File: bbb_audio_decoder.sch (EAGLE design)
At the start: 186 parts, among them IC1 OPA2134, IC2 LM317, IC3 LM337, IC4 OPA2134, IC5 OPA2134, IC6 OPA2134, IC7 LM317, P1 PLR135/T9, Q2 BS170, U1 PCM1690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

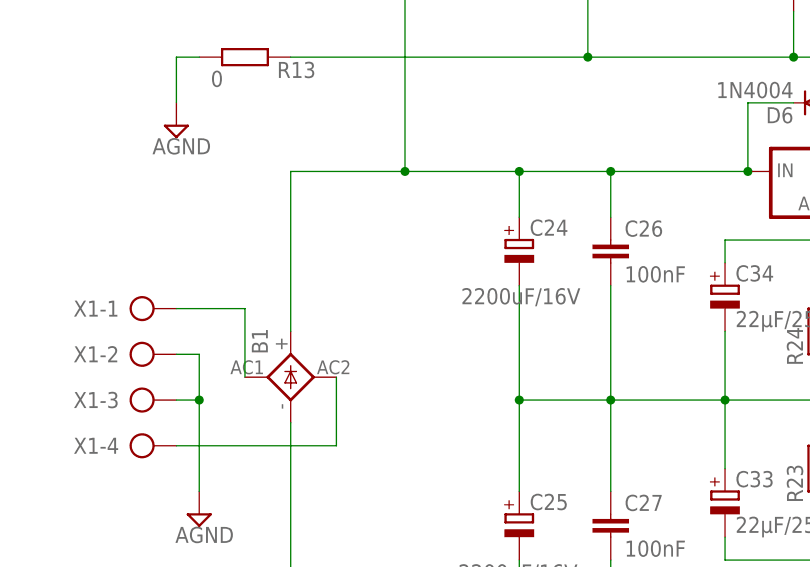
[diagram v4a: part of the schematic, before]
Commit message: Add another power supply cap to fix boot problems
The extra cap (C17) is 2200µF.

The problem was that it sometimes refused to boot. I saw the
BeagleBone's blue lights go off again when the boot process was
initiated. The LCD backlight dipped. Scope image revealved dips in the
rail, together with 100Hz rectification ripple. As a hack to my build, I
added 4700µF before the positive regulators.  That prevented the
dips. I'm not sure if this one extra 2200µF is enough though. Probably
it is, and there are space constraints.
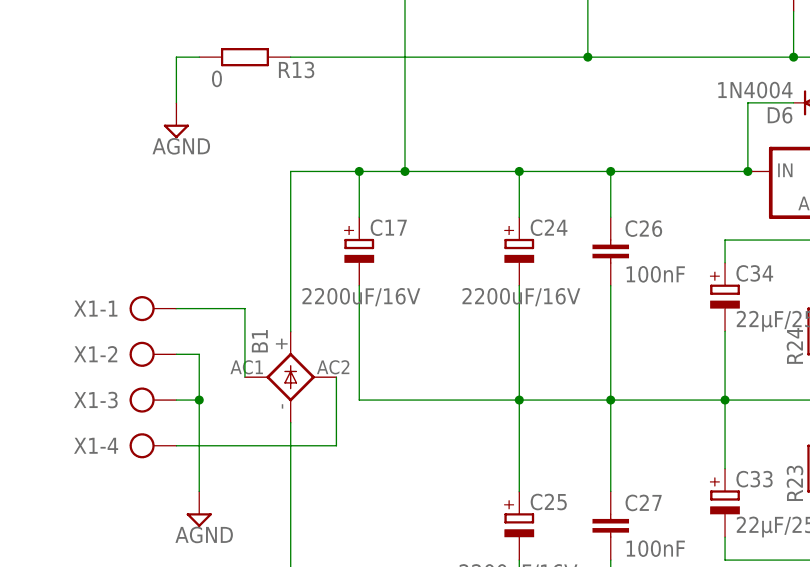
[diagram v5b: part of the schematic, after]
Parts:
- added C17: 2200uF/16V, rcl:CPOL-EUE5-13
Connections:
- net AGND: now also C17.-
- net N$39: now also C17.+
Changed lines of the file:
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@@
 <part name="SUPPLY57" library="supply2" deviceset="+5V/1" device=""/>
 <part name="LED1" library="led" deviceset="LED" device="SMT1206"/>
+<part name="C17" library="rcl" deviceset="CPOL-EU" device="E5-13" value="2200uF/16V"/>
 </parts>
 <sheets>
@@
 <instance part="SUPPLY57" gate="G$1" x="7.62" y="-43.18" rot="R180"/>
 <instance part="LED1" gate="G$1" x="5.08" y="132.08"/>
+<instance part="C17" gate="G$1" x="15.24" y="233.68" smashed="yes">
+<attribute name="NAME" x="16.383" y="234.1626" size="1.778" layer="95"/>
+<attribute name="VALUE" x="8.763" y="226.5426" size="1.778" layer="96"/>
+</instance>
 </instances>
 <busses>
@@
 <wire x1="116.84" y1="215.9" x2="114.3" y2="215.9" width="0.1524" layer="91"/>
 <junction x="114.3" y="215.9"/>
+<pinref part="C17" gate="G$1" pin="-"/>
+<wire x1="15.24" y1="228.6" x2="15.24" y2="215.9" width="0.1524" layer="91"/>
+<wire x1="15.24" y1="215.9" x2="33.02" y2="215.9" width="0.1524" layer="91"/>
 </segment>
 <segment>
@@
 <pinref part="B1" gate="1" pin="+"/>
 <wire x1="7.62" y1="223.52" x2="7.62" y2="241.3" width="0.1524" layer="91"/>
-<wire x1="7.62" y1="241.3" x2="20.32" y2="241.3" width="0.1524" layer="91"/>
+<wire x1="7.62" y1="241.3" x2="15.24" y2="241.3" width="0.1524" layer="91"/>
+<wire x1="15.24" y1="241.3" x2="20.32" y2="241.3" width="0.1524" layer="91"/>
 <wire x1="20.32" y1="241.3" x2="33.02" y2="241.3" width="0.1524" layer="91"/>
 <wire x1="40.64" y1="281.94" x2="55.88" y2="281.94" width="0.1524" layer="91"/>
@@
 <junction x="20.32" y="241.3"/>
 <junction x="20.32" y="281.94"/>
-</segment>
-</net>
+<pinref part="C17" gate="G$1" pin="+"/>
+<wire x1="15.24" y1="236.22" x2="15.24" y2="241.3" width="0.1524" layer="91"/>
+<junction x="15.24" y="241.3"/>
+</segment>
+</net>
